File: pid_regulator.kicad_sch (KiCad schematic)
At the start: 13 parts, among them J1 Screw_Terminal_01x02, J2 Screw_Terminal_01x02, K1 Fujitsu_FTR-LYCA005x, Q1 BC847, U2 YD-ESP32-S3

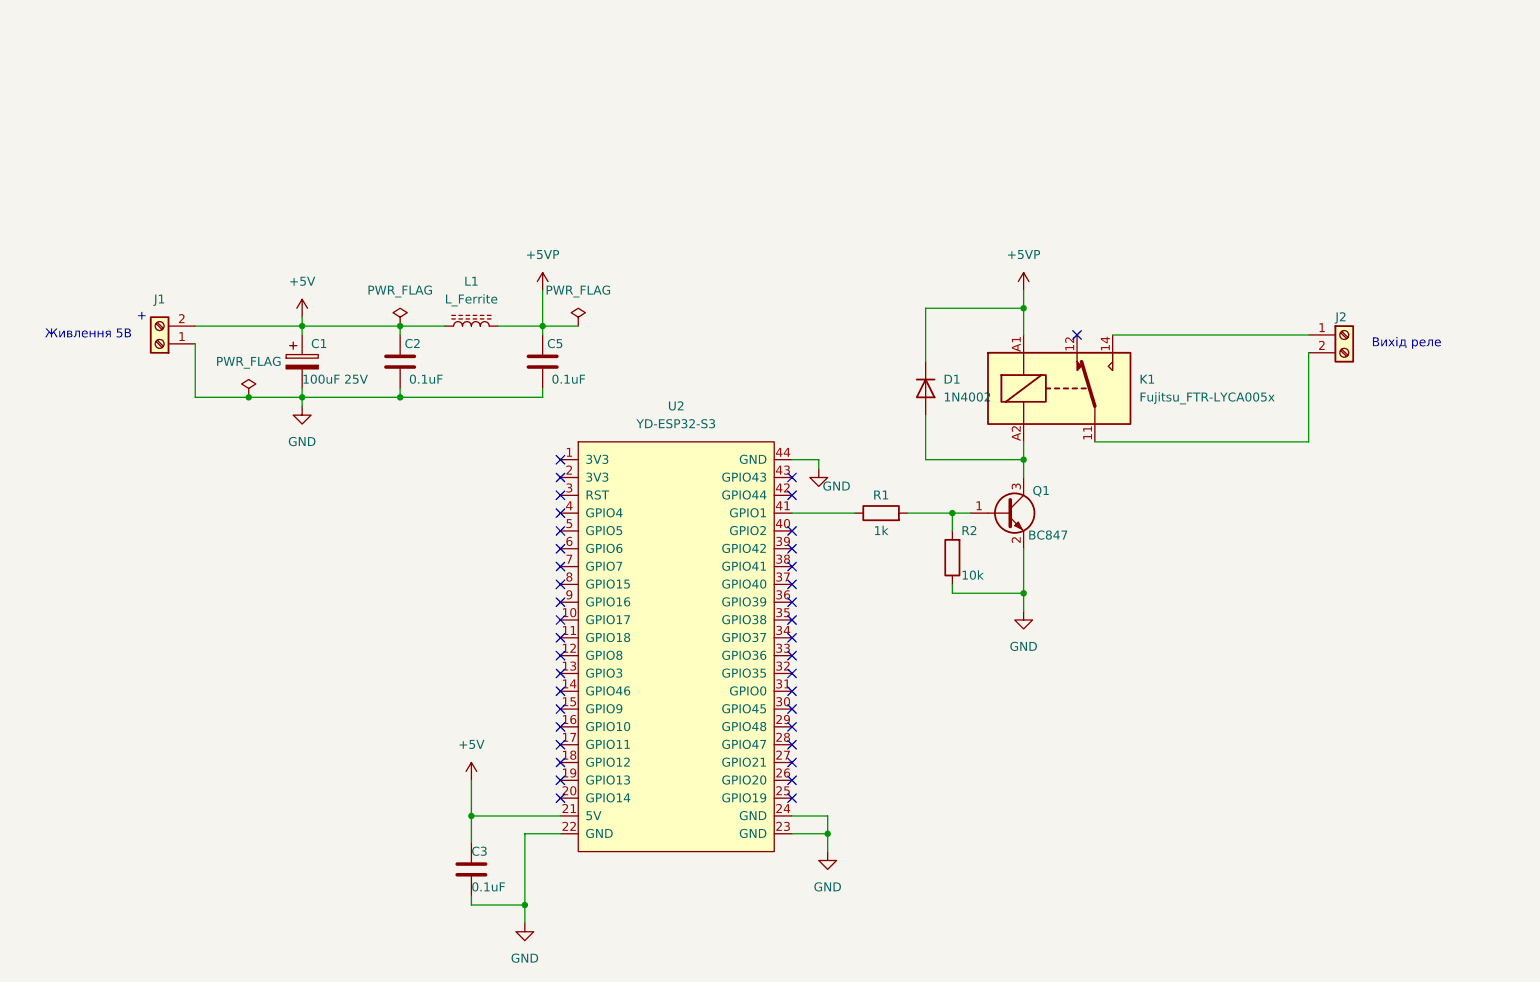
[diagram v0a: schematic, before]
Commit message: Add PID regulator schematic
Signed-off-by: Volodymyr Kaliuzhnyi <vladimirvk2007@gmail.com>
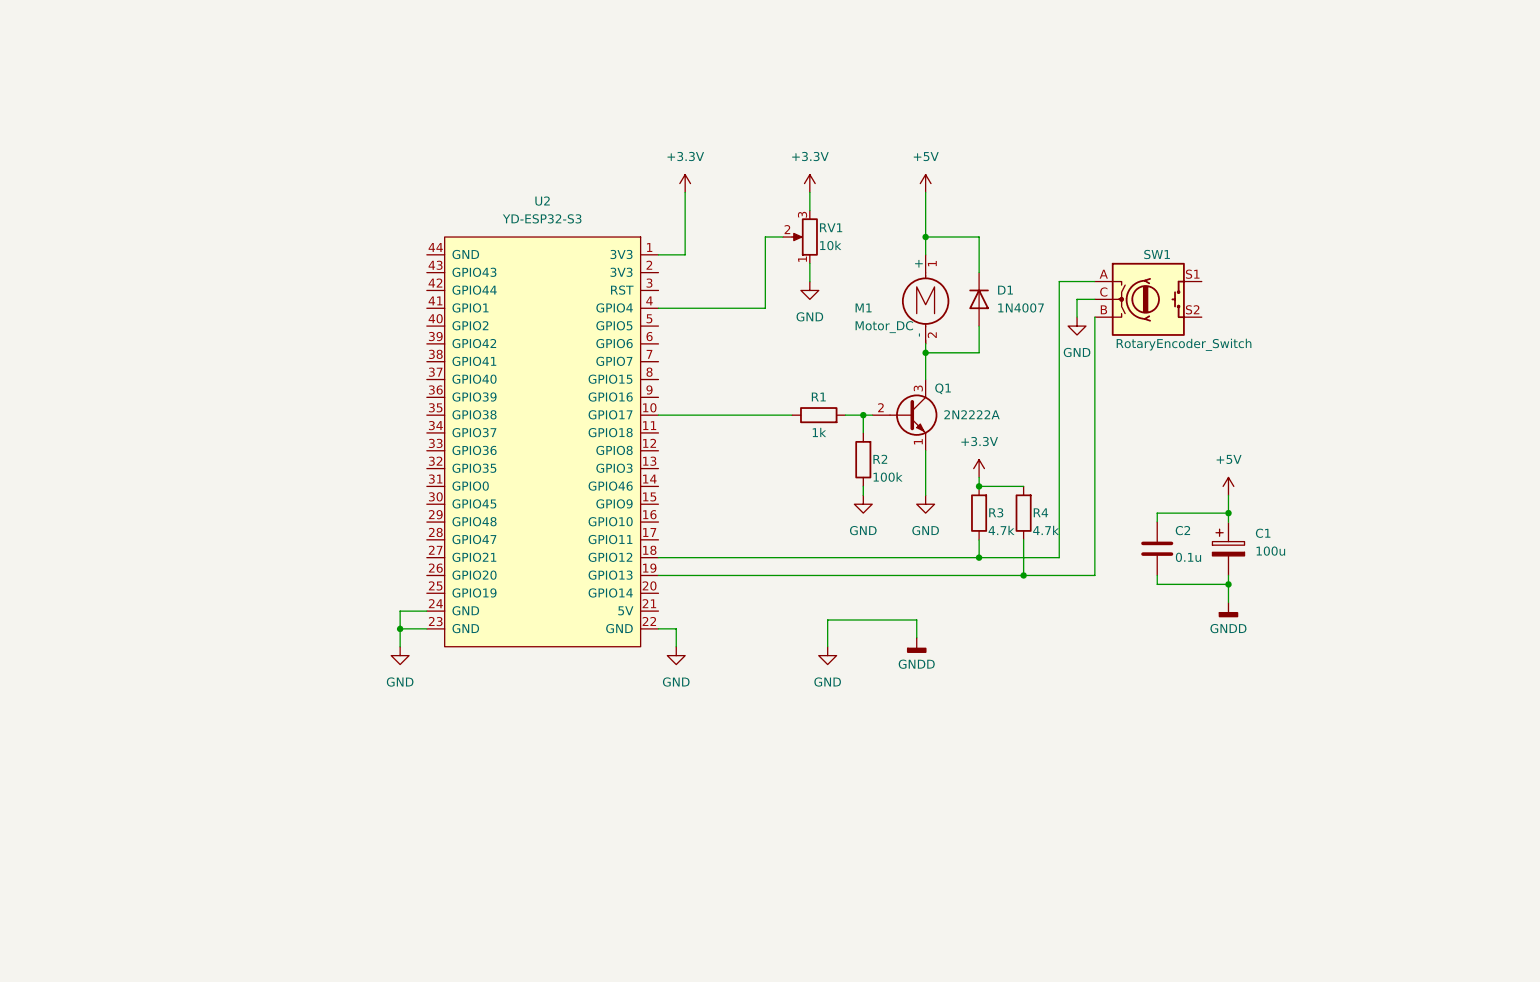
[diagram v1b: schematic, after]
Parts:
- removed C3, C5: 0.1uF, Capacitor_SMD:C_1206_3216Metric, symbol Device:C
- removed D1: 1N4002, Diode_THT:D_DO-41_SOD81_P10.16mm_Horizontal, symbol Diode:1N4002
- removed J1, J2: Screw_Terminal_01x02, TerminalBlock_Phoenix:TerminalBlock_Phoenix_MKDS-1,5-2-5.08_1x02_P5.08mm_Horizontal, symbol Connector:Screw_Terminal_01x02
- removed K1: Fujitsu_FTR-LYCA005x, Relay_THT:Relay_SPDT_Fujitsu_FTR-LYCA005x_FormC_Vertical, symbol Relay:Fujitsu_FTR-LYCA005x
- removed L1: L_Ferrite, Inductor_SMD:L_2512_6332Metric_Pad1.52x3.35mm_HandSolder, symbol Device:L_Ferrite
- removed Q1: BC847, Package_TO_SOT_SMD:SOT-23, symbol Transistor_BJT:BC847
- removed U2: YD-ESP32-S3, My_Library:YD-ESP32-S3, symbol My_Parts:YD-ESP32-S3
- added D1: 1N4007, Diode_THT:D_DO-41_SOD81_P10.16mm_Horizontal, symbol Diode:1N4007
- added M1: Motor_DC, symbol Motor:Motor_DC
- added Q1: 2N2222A, Package_TO_SOT_THT:TO-39-3, symbol Transistor_BJT:2N2219
- added R3, R4: 4.7k, symbol Device:R
- added RV1: 10k, symbol Device:R_Potentiometer
- added SW1: RotaryEncoder_Switch, symbol Device:RotaryEncoder_Switch
- added U2: YD-ESP32-S3, Shared:YD-ESP32-S3, symbol YD-ESP32-S3:YD-ESP32-S3
- C1: value 100uF 25V -> 100u; footprint Capacitor_THT:CP_Radial_D6.3mm_P2.50mm -> (none)
- C2: value 0.1uF -> 0.1u; footprint Capacitor_SMD:C_1206_3216Metric -> (none)
- R1: footprint Resistor_SMD:R_1206_3216Metric_Pad1.30x1.75mm_HandSolder -> (none)
- R2: value 10k -> 100k; footprint Resistor_SMD:R_1206_3216Metric -> (none)
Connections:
- net +5V: now also D1.1 (K), M1.1 (+)
- net GND: now also Q1.1 (E), RV1.1, SW1.C, U2.22 (GND), U2.23 (GND), U2.24 (GND)
- net at R1.1: now also U2.10 (GPIO17)
- net at R1.2, R2.2: now also Q1.2 (B)
- new net: R4.1, SW1.B, U2.19 (GPIO13)
- new net: R3.1, SW1.A, U2.18 (GPIO12)
- new net: RV1.2, U2.4 (GPIO4)
- new net: D1.2 (A), M1.2 (-), Q1.3 (C)
- new net +3.3V: R3.2, R4.2, RV1.3, U2.1 (3V3)
- no-connect marks 39 -> 0
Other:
- note removed: "+"
- note removed: "Вихід реле"
- note removed: "Живлення 5В"
- company: Beetroot -> (none)
- title: Example -> PID Regulator

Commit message: Some minor changes
Signed-off-by: Volodymyr Kaliuzhnyi <vladimirvk2007@gmail.com>
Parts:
- added D1, D3, D4, D5: 1N4007, Diode_THT:D_DO-41_SOD81_P10.16mm_Horizontal, symbol Diode:1N4007
- added K1: G5V-2, Relay_THT:Relay_DPDT_Omron_G5V-2, symbol Relay:G5V-2
- added Q2: BC847, Package_TO_SOT_SMD:SOT-23, symbol Transistor_BJT:BC847
- added R5: 1k, symbol Device:R
- added R6: 100k, symbol Device:R
- renumbered C2 to C1, C1 to C2, D1 to D2, R3 to R1, R4 to R2, R1 to R3, R2 to R4
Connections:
- net +5V: now also D1.1 (K), D4.1 (K), K1.11, K1.16, K1.8; no longer M1.1 (+)
- net GND: now also D3.2 (A), D5.2 (A), Q2.2 (E), R6.1
- net at U2.7 (GPIO7): now also R5.1
- new net: D3.1 (K), D4.2 (A), K1.4, M1.2 (-)
- new net: Q2.1 (B), R5.2, R6.2
- new net: D2.2 (A), D5.1 (K), K1.13, M1.1 (+)
- new net: D1.2 (A), K1.1, Q2.3 (C)
- new net: K1.6, K1.9, Q1.3 (C)
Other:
- title: PID Regulator -> PID Regulator (Both Directions)
- moved on the sheet: C1, C2, D2, M1, Q1, R1, R2, R3, R4, RV1, SW1, U2
